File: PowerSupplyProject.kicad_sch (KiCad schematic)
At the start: 17 parts, among them J1 Conn_01x02_Pin, J2 Conn_01x02_Pin, J3 Conn_01x03_Pin, J4 Conn_01x03_Pin, J5 Screw_Terminal_01x02, J7 Screw_Terminal_01x02, J8 Barrel_Jack_Switch, SW1 EG1218, U1 LM7805_TO220, U2 LM317_TO-220

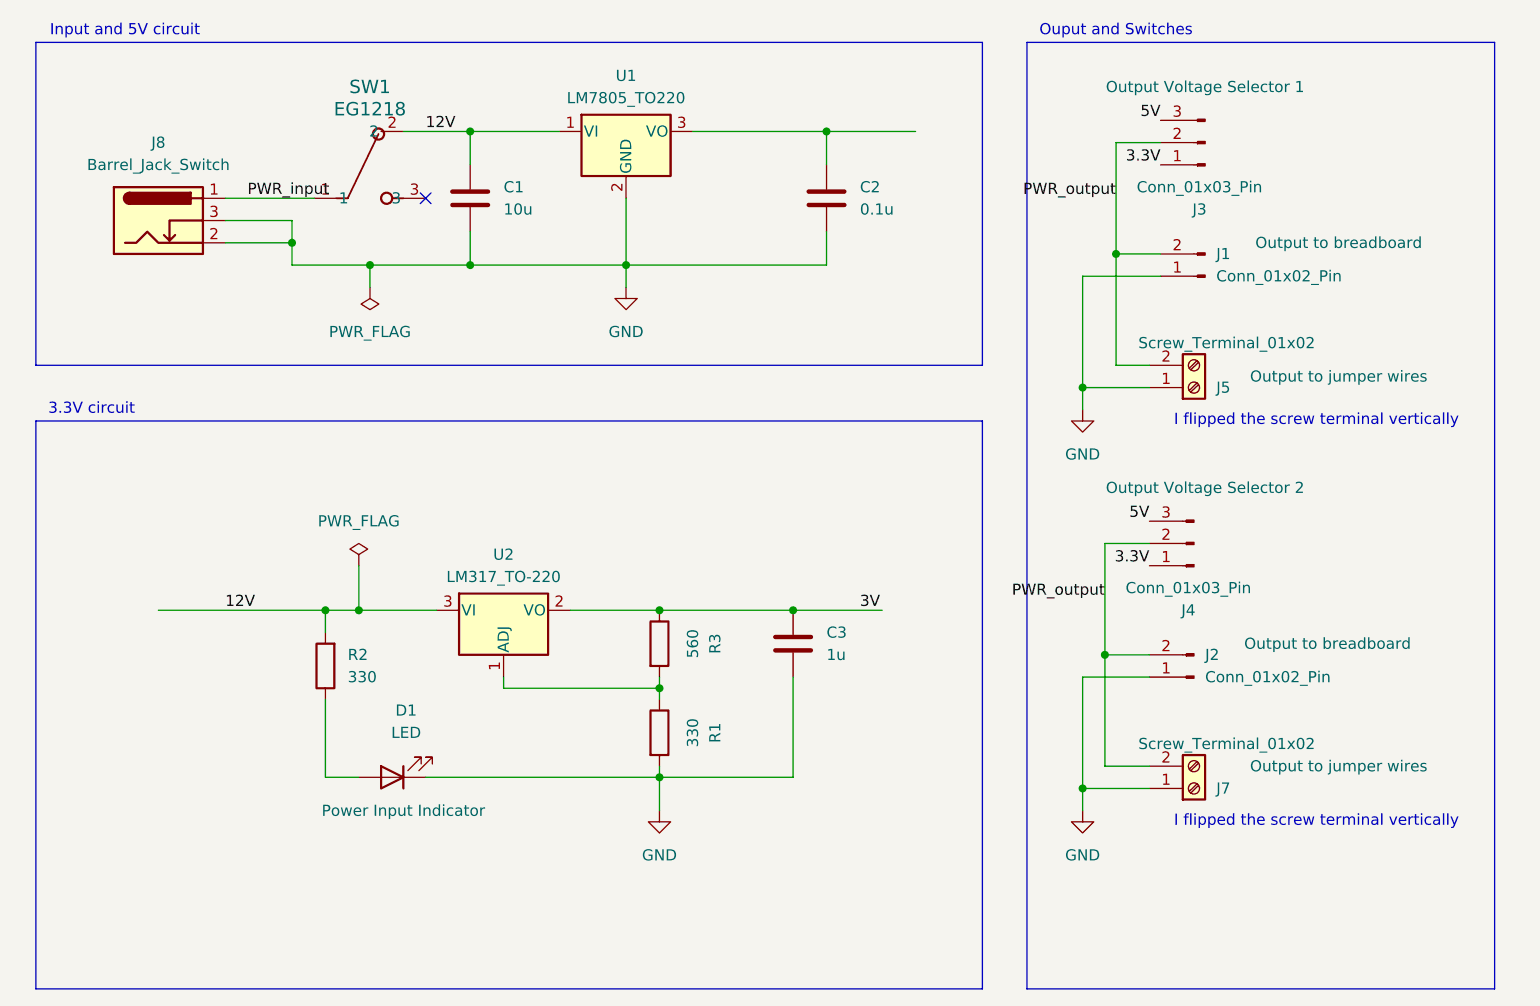
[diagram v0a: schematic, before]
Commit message: fixed the schematic label and value components
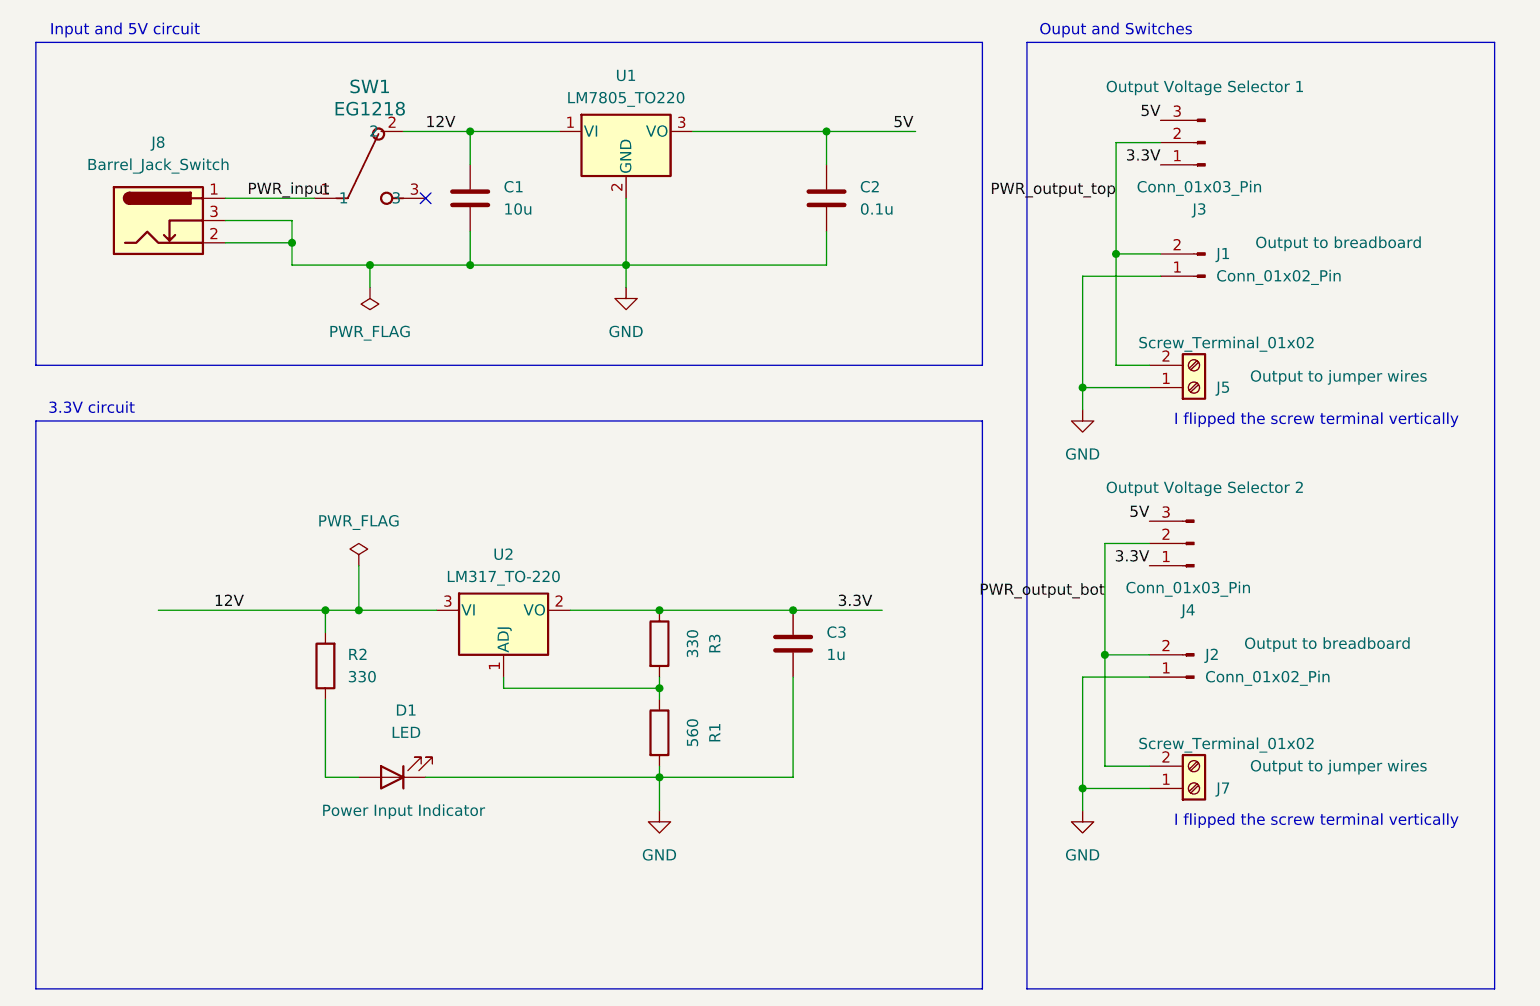
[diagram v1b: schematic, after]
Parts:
- R1: value 330 -> 560
- R3: value 560 -> 330
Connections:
- net 3V is gone; now on net 3.3V: C3.1, R3.1, U2.2 (VO)
- net 5V: now also C2.1, U1.3 (VO)
- net PWR_output renamed PWR_output_bot
- net PWR_output_bot: no longer J1.2 (Pin_2), J3.2 (Pin_2), J5.2 (Pin_2)
- new net PWR_output_top: J1.2 (Pin_2), J3.2 (Pin_2), J5.2 (Pin_2)
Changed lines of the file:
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@@
 		)
 	)
-	(label "PWR_output"
+	(label "12V"
+		(at 82.55 109.22 0)
+		(effects
+			(font
+				(size 1.27 1.27)
+			)
+			(justify left bottom)
+		)
+	)
+	(label "PWR_output_bot"
 		(at 184.15 107.95 180)
 		(effects
@@
 		)
 	)
-	(label "PWR_output"
+	(label "3.3V"
+		(at 153.67 109.22 0)
+		(effects
+			(font
+				(size 1.27 1.27)
+			)
+			(justify left bottom)
+		)
+	)
+	(label "PWR_output_top"
 		(at 185.42 62.23 180)
 		(effects
@@
 			)
 			(justify right bottom)
-		)
-	)
-	(label "12V"
-		(at 83.82 109.22 0)
-		(effects
-			(font
-				(size 1.27 1.27)
-			)
-			(justify left bottom)
 		)
 	)
@@
 		)
 	)
-	(label "3V"
-		(at 156.21 109.22 0)
-		(effects
-			(font
-				(size 1.27 1.27)
-			)
-			(justify left bottom)
-		)
-	)
 	(label "5V"
 		(at 189.23 99.06 180)
@@
 			)
 			(justify right bottom)
+		)
+	)
+	(label "5V"
+		(at 160.02 54.61 0)
+		(effects
+			(font
+				(size 1.27 1.27)
+			)
+			(justify left bottom)
 		)
 	)
@@
 			)
 		)
-		(property "Value" "330"
+		(property "Value" "560"
 			(at 137.16 123.19 90)
 			(show_name no)
@@
 			)
 		)
-		(property "Value" "560"
+		(property "Value" "330"
 			(at 137.16 113.03 90)
 			(show_name no)

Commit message: fix route based on fixed label
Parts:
- R1: value 560 -> 330
- R3: value 330 -> 560
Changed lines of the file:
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@@
 			)
 		)
-		(property "Value" "560"
+		(property "Value" "330"
 			(at 137.16 123.19 90)
 			(show_name no)
@@
 			)
 		)
-		(property "Value" "330"
+		(property "Value" "560"
 			(at 137.16 113.03 90)
 			(show_name no)
